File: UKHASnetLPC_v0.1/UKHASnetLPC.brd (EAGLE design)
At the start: 46.7 x 26.7 mm, 9 parts

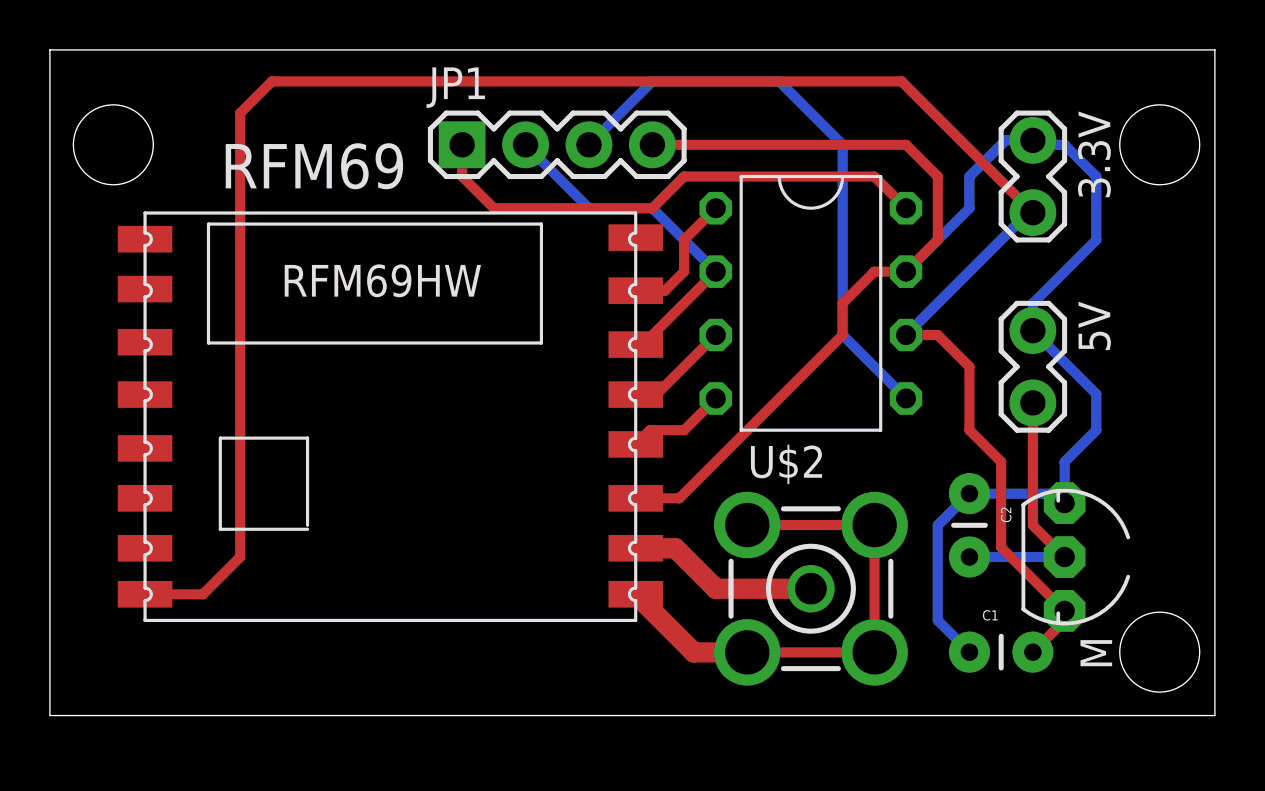
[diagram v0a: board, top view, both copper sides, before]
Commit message: Redesigned board to avoid interference
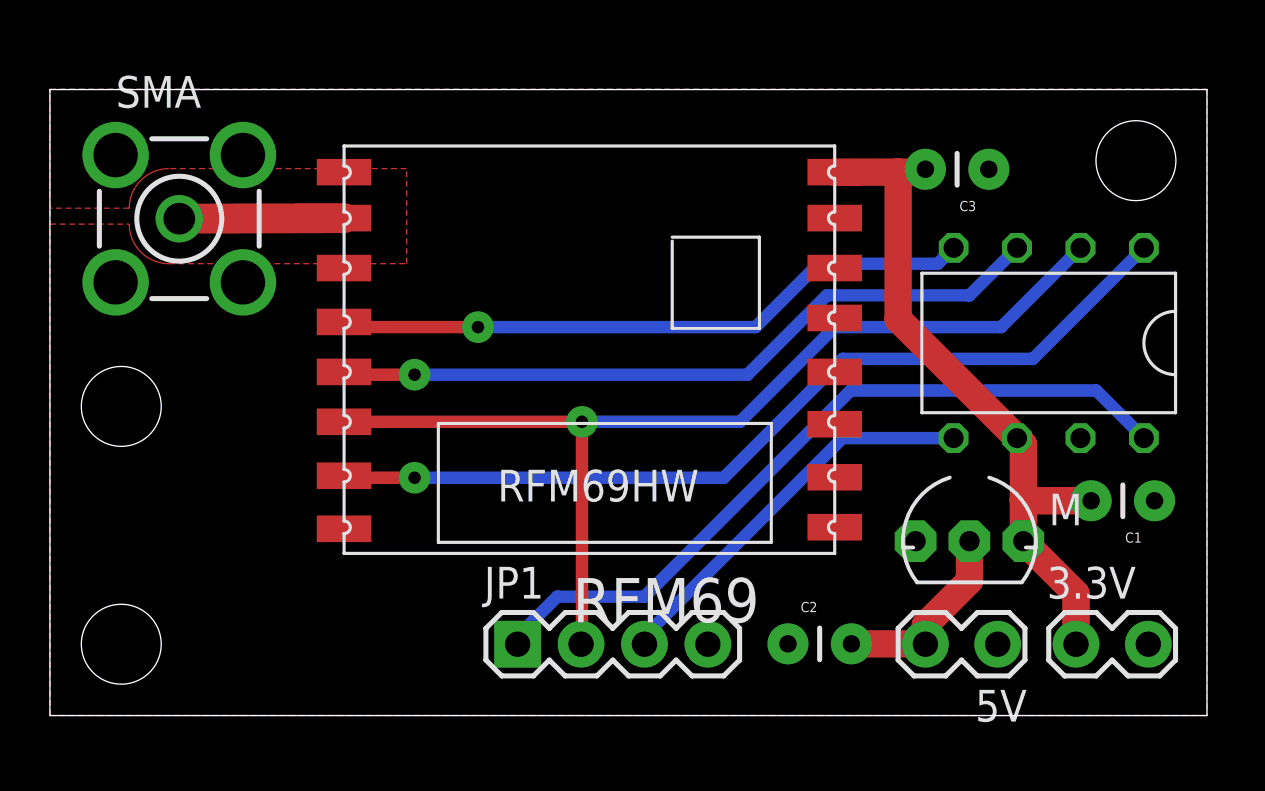
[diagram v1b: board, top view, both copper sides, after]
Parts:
- removed U$2: (no value), Ava:BUS-SMA
- added C3: 1uF, SparkFun-Capacitors:CAP-PTH-SMALL
- added SMA: (no value), Ava:BUS-SMA
- C1, C2: value (none) -> 1uF
- moved RFM69 33.5 mm to (31.4, 22.8), turned to 180 degrees
- moved JP1 20.1 mm to (18.7, 2.86)
- moved 3.3V 20.1 mm to (41.3, 2.86), turned to 0 degrees
- moved 5V 12.5 mm to (37.8, 2.86), turned to 180 degrees
- moved LPC810 9.66 mm to (40.0, 14.9), turned to 270 degrees
- moved C1 9.58 mm to (44.2, 8.60), turned to 180 degrees
- moved C2 9.44 mm to (29.6, 2.87), turned to 0 degrees
- moved M 3.86 mm to (36.8, 6.99), turned to 0 degrees
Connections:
- removed net N$12: 3.3V.2, C1.2, LPC810.P$6, M.3, RFM69.VCC
- removed net N$5: 3.3V.1, 5V.1, C1.1, C2.1, JP1.4, LPC810.P$7, M.1, RFM69.GNDA
- new net VCC: 3.3V.1, C1.2, C3.2, LPC810.P$6, M.3, RFM69.VCC
- net GND: now also 3.3V.2, 5V.1, C1.1, C2.1, C3.1, JP1.4, LPC810.P$7, M.1, RFM69.GNDA, SMA.2, SMA.3, SMA.4, SMA.5; no longer U$2.2, U$2.3, U$2.4, U$2.5
- net N$10: now also SMA.1; no longer U$2.1
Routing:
- net N$12: track 80.4 -> 0.00 mm
- net N$5: track 69.8 -> 0.00 mm
- net N$1: track 5.32 -> 35.9 mm, vias 0 -> 1
- net VCC: track 0.00 -> 28.3 mm
- net N$2: track 14.1 -> 41.3 mm, vias 0 -> 1
- net N$3: track 4.33 -> 29.1 mm, vias 0 -> 1
- net N$4: track 3.97 -> 25.8 mm, vias 0 -> 1
- net GND: track 20.7 -> 0.00 mm
- net N$7: track 20.6 -> 30.3 mm
- net N$6: track 23.5 -> 16.0 mm
- net N$11: track 10.5 -> 7.83 mm
- net N$10: track 7.69 -> 6.60 mm
- added copper zone on layer 1, net GND
- added copper zone on layer 16, net GND
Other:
- board size 46.7 x 26.7 mm -> 46.3 x 25.1 mm
- board text added: "UKHASnet"
- board text added: "v0.1"
- board text removed: "UKHASnet 0.1"
